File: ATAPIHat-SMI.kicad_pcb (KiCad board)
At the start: 2 copper layers, 65 x 56 mm, 35 parts, among them J1 Pi, J2 IDE, U1 AT24CS32, U2 TXS0108EPW, U3 MCP23S17_SO, U4 MCP23S17_SO

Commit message: Do layout
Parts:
- removed ? (x4): , RPi_Hat:RPi_Hat_Mounting_Hole
- removed D2, D3: Red, LED_SMD:LED_0603_1608Metric
- removed D4, D5: Yellow, LED_SMD:LED_0603_1608Metric
- removed D6, D7: Green, LED_SMD:LED_0603_1608Metric
- removed D8, D9: Blue, LED_SMD:LED_0603_1608Metric
- removed U1: AT24CS32, Package_SO:SOIC-8_3.9x4.9mm_P1.27mm
- removed U2: TXS0108EPW, Package_SO:TSSOP-20_4.4x6.5mm_P0.65mm
- removed U3, U4: MCP23S17_SO, Package_SO:SOIC-28W_7.5x17.9mm_P1.27mm
- added C6: 22uF, Capacitor_SMD:C_0805_2012Metric, F.Cu at (78.8, 159.9)
- added J3: Conn_01x03_Male, Jumper:SolderJumper-3_P1.3mm_Bridged12_Pad1.0x1.5mm, F.Cu at (52.0, 141.9)
- added R12: 33R, Resistor_SMD:R_0402_1005Metric, F.Cu at (100.2, 139.0)
- added R13: 33R, Resistor_SMD:R_0402_1005Metric, F.Cu at (71.0, 136.2)
- added R14: 22R, Resistor_SMD:R_0402_1005Metric, F.Cu at (74.8, 139.0)
- added R15: 33R, Resistor_SMD:R_0402_1005Metric, F.Cu at (99.0, 136.2)
- added R16: 10k, Resistor_SMD:R_0402_1005Metric, F.Cu at (63.4, 139.0)
- added R17: 4.7k, Resistor_SMD:R_0402_1005Metric, F.Cu at (77.3, 139.0)
- added R18: 10k, Resistor_SMD:R_0402_1005Metric, F.Cu at (69.7, 136.2)
- added R19: 5.6k, Resistor_SMD:R_0402_1005Metric, F.Cu at (83.7, 136.2)
- added R20: 75R, Resistor_SMD:R_0402_1005Metric, F.Cu at (86.3, 136.2)
- added R21: 33R, Resistor_SMD:R_0402_1005Metric, F.Cu at (55.8, 136.2)
- added R22: 33R, Resistor_SMD:R_0402_1005Metric, F.Cu at (60.9, 136.2)
- added R23: 22R, Resistor_SMD:R_0402_1005Metric, F.Cu at (91.4, 136.2)
- added R24: 33R, Resistor_SMD:R_0402_1005Metric, F.Cu at (82.5, 139.0)
- added R25: 33R, Resistor_SMD:R_0402_1005Metric, F.Cu at (76.1, 136.2)
- added R26: 33R, Resistor_SMD:R_0402_1005Metric, F.Cu at (92.6, 139.0)
- added R27: 33R, Resistor_SMD:R_0402_1005Metric, F.Cu at (87.5, 139.0)
- added R28: 33R, Resistor_SMD:R_0402_1005Metric, F.Cu at (58.4, 136.2)
- added R29: 33R, Resistor_SMD:R_0402_1005Metric, F.Cu at (88.8, 136.2)
- added R30: 22R, Resistor_SMD:R_0402_1005Metric, F.Cu at (85.0, 139.0)
- added R31: 33R, Resistor_SMD:R_0402_1005Metric, F.Cu at (78.7, 136.2)
- added R32: 33R, Resistor_SMD:R_0402_1005Metric, F.Cu at (81.2, 136.2)
- added R33: 33R, Resistor_SMD:R_0402_1005Metric, F.Cu at (93.9, 136.2)
- C1: value 100n -> 100nF
- C2, C3, C4, C5: value 100n -> 22uF; footprint Capacitor_SMD:C_0402_1005Metric -> Capacitor_SMD:C_0805_2012Metric
- R1, R10, R11, R2, R4, R5, R6: value 4.7k -> 33R
- R7: value 4.7k -> 75R
- R8: value 10k -> 75R
- R9: value 10k -> 33R
- moved R3 53.9 mm to (52.0, 180.6), turned to 0 degrees
- moved D1 53.8 mm to (55.6, 180.6)
- moved J2 47.9 mm to (102.1, 172.3), turned to 270 degrees
- moved R1 34.3 mm to (64.7, 139.0), turned to 90 degrees
- moved R2 33.1 mm to (66.0, 136.2), turned to 90 degrees
- moved C5 32.1 mm to (78.8, 161.8)
- moved C3 24.5 mm to (78.8, 165.6), turned to 0 degrees
- moved C4 23.8 mm to (78.8, 163.7), turned to 0 degrees
- moved R9 23.8 mm to (62.1, 139.0), turned to 90 degrees
- moved R8 20.8 mm to (68.5, 136.2)
- moved C2 18.8 mm to (78.8, 167.5)
- moved R10 18.2 mm to (97.7, 139.0), turned to 90 degrees
- moved R6 18.2 mm to (72.3, 139.0), turned to 90 degrees
- moved R5 17.2 mm to (102.8, 139.0), turned to 90 degrees
- moved R11 17.1 mm to (67.2, 139.0), turned to 90 degrees
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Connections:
- C1 pad 1: +5V -> +3V3
- C2 pad 1: +5V -> /VDRIVE
- C3 pad 1: +5V -> /VDRIVE
- C4 pad 1: +3V3 -> /VDRIVE
- C5 pad 1: +3V3 -> /VDRIVE
- D1 pad 2: +5V -> +3V3
- J1 pad 19: /3V_MOSI -> Net-(J1-Pad19)
- J1 pad 21: /3V_MISO -> Net-(J1-Pad21)
- J1 pad 23: /3V_SCK -> Net-(J1-Pad23)
- J1 pad 24: /3V_CE0 -> Net-(J1-Pad24)
- J1 pad 26: /3V_CE1 -> Net-(J1-Pad26)
- J1 pad 27: /ID_SD -> Net-(J1-Pad27)
- J1 pad 28: /ID_SC -> Net-(J1-Pad28)
- J2 pad 1: +5V -> /RESET
- J2 pad 20: Net-(J2-Pad20) -> /VDRIVE
- J2 pad 21: +5V -> /DMA_RQ
- J2 pad 28: Net-(J2-Pad28) -> GND
- J2 pad 29: +5V -> /DMA_ACK
- R1 pad 1: +3V3 -> /D7
- R1 pad 2: /ID_SD -> Net-(J1-Pad10)
- R10 pad 1: Net-(D8-Pad1) -> /D8
- R10 pad 2: Net-(R10-Pad2) -> Net-(J1-Pad36)
- R11 pad 1: Net-(D9-Pad1) -> /D10
- R11 pad 2: Net-(R11-Pad2) -> Net-(J1-Pad12)
- R2 pad 1: +3V3 -> /D9
- R2 pad 2: /ID_SC -> Net-(J1-Pad11)
- R3 pad 1: Net-(D1-Pad1) -> /ACTIVE
- R3 pad 2: /ACTIVE -> Net-(D1-Pad1)
- R4 pad 1: Net-(D2-Pad1) -> /D11
- R4 pad 2: Net-(R4-Pad2) -> Net-(J1-Pad35)
- R5 pad 1: Net-(D3-Pad1) -> /D13
- R5 pad 2: Net-(R5-Pad2) -> Net-(J1-Pad40)
- R6 pad 1: Net-(D4-Pad1) -> /D15
- R6 pad 2: Net-(R6-Pad2) -> Net-(J1-Pad16)
- R7 pad 1: Net-(D5-Pad1) -> Net-(J1-Pad22)
- R7 pad 2: Net-(R7-Pad2) -> /IO_CH_RD
- R8 pad 1: Net-(D6-Pad1) -> Net-(J1-Pad13)
- R8 pad 2: Net-(R8-Pad2) -> /IRQ
- R9 pad 1: Net-(D7-Pad1) -> /D6
- R9 pad 2: Net-(R9-Pad2) -> Net-(J1-Pad8)
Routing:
- net +5V: track 202.0 -> 15.0 mm, vias 3 -> 0
- net /VDRIVE: track 0.00 -> 70.3 mm, vias 0 -> 5
- net /D9: track 10.4 -> 68.5 mm, vias 0 -> 2
- net /MISO: track 53.3 -> 0.00 mm, vias 3 -> 0
- net /D10: track 10.9 -> 62.0 mm, vias 0 -> 2
- net /CS1: track 18.8 -> 68.5 mm, vias 0 -> 2
- net /MOSI: track 48.4 -> 0.00 mm, vias 5 -> 0
- net /SCK: track 46.7 -> 0.00 mm, vias 4 -> 0
- net /DMA_RQ: track 0.00 -> 45.1 mm, vias 0 -> 2
- net /D6: track 23.3 -> 67.9 mm, vias 0 -> 2
- net /D7: track 23.4 -> 68.0 mm, vias 0 -> 2
- net /DA0: track 20.9 -> 65.4 mm, vias 0 -> 2
- net /IO_CH_RD: track 0.00 -> 43.8 mm, vias 0 -> 2
- net /CE0: track 42.4 -> 0.00 mm, vias 4 -> 0
- net /IOR: track 13.8 -> 55.2 mm, vias 0 -> 2
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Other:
- board text added: "3.3V"
- board text added: "5V"
- board text added: "ATA/ATAPI Hat SMI Rev. A 2020 Tobias Mädel Tobias Schramm"
- board text added: "Activity"
- board text removed: "ATA/ATAPI Hat Rev. B Tobias Mädel 2020"

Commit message: Center hat name
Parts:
- removed C3, C4, C5, C6: 22uF, Capacitor_SMD:C_0805_2012Metric
- added ?: , RPi_Hat:RPi_Hat_Mounting_Hole, F.Cu at (48.4, 131.7)
- added ?: , RPi_Hat:RPi_Hat_Mounting_Hole, F.Cu at (106.4, 180.7)
- added ?: , RPi_Hat:RPi_Hat_Mounting_Hole, F.Cu at (48.4, 180.7)
- added ?: , RPi_Hat:RPi_Hat_Mounting_Hole, F.Cu at (106.4, 131.7)
- moved R3 0.63 mm to (52.6, 180.6)
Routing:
- net /VDRIVE: track 70.3 -> 61.7 mm
- net Net-(D1-Pad1): track 2.69 -> 2.05 mm
- net GND: vias 170 -> 164

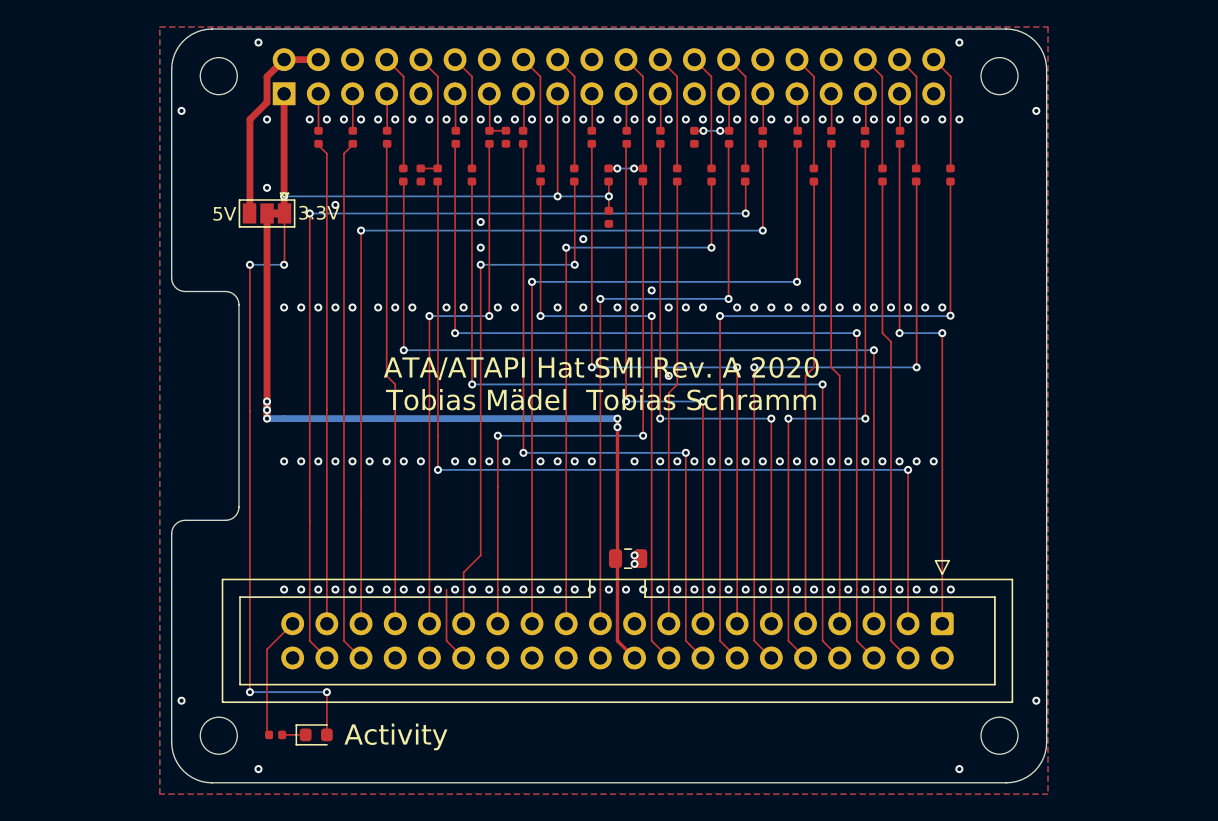
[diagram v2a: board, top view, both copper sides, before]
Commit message: Add tooling holes
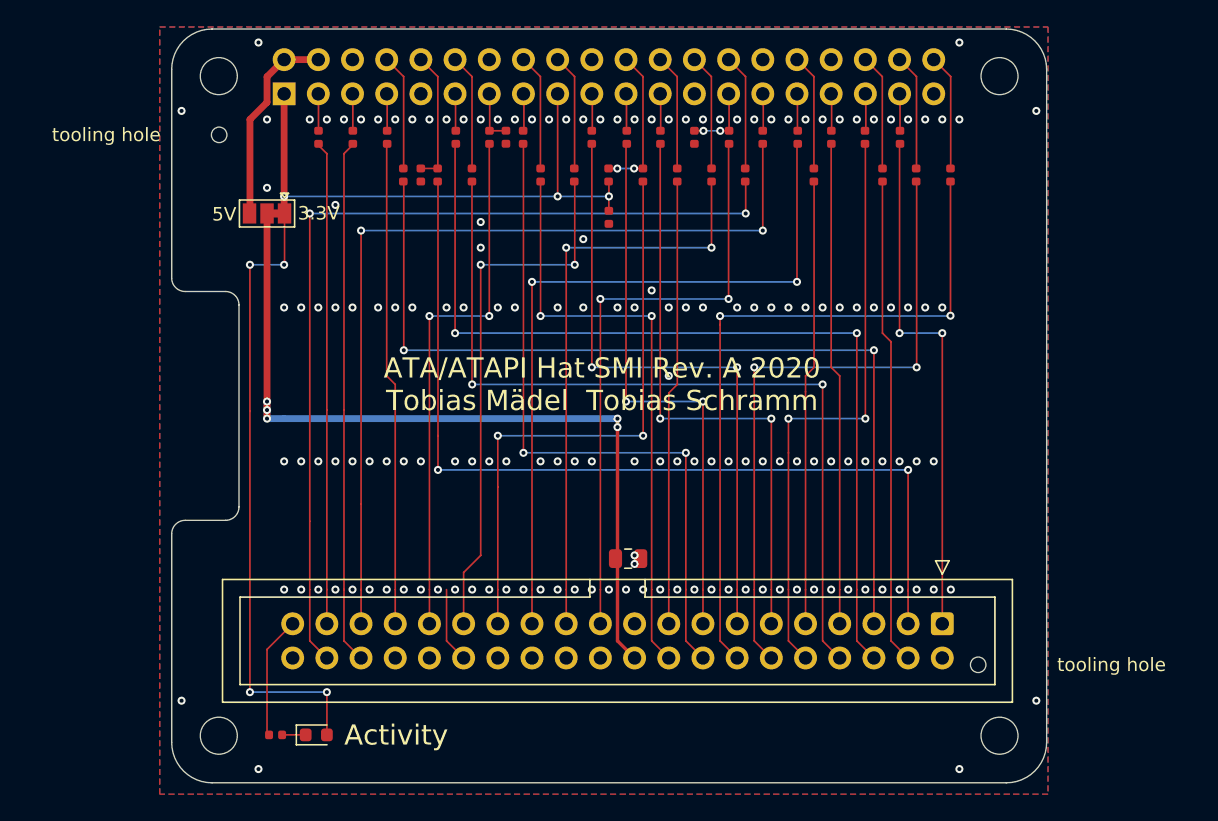
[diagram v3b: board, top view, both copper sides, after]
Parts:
- added H1: ToolingHole, ToolingHole:ToolingHole_JLCSMT, F.Cu at (48.4, 136.0)
- added H2: ToolingHole, ToolingHole:ToolingHole_JLCSMT, F.Cu at (104.8, 175.4)
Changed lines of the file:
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@@
     (tracks 447)
     (zones 0)
-    (modules 43)
+    (modules 45)
     (nets 65)
   )
@@
       (drillshape 0)
       (scaleselection 1)
-      (outputdirectory "IDEHat/"))
+      (outputdirectory "fab"))
   )
   (net 0 "")
@@
     (add_net "Net-(J2-Pad34)")
   )
+  (module ToolingHole:ToolingHole_JLCSMT (layer F.Cu)
+    (at 104.807628 175.387876)
+    (fp_text reference H2 (at 0 0.5) (layer F.SilkS) hide
+      (effects (font (size 1 1) (thickness 0.15)))
+    )
+    (fp_text value ToolingHole (at 0 -0.5) (layer F.Fab)
+      (effects (font (size 1 1) (thickness 0.15)))
+    )
+    (fp_text user "tooling hole" (at 9.906 0) (layer F.SilkS)
+      (effects (font (size 1 1) (thickness 0.15)))
+    )
+    (pad "" np_thru_hole circle (at 0 0) (size 1.152 1.152) (drill 1.152) (layers *.Cu *.Mask))
+  )
+  (module ToolingHole:ToolingHole_JLCSMT (layer F.Cu)
+    (at 48.419628 136.017876)
+    (fp_text reference H1 (at 0 0.5) (layer F.SilkS) hide
+      (effects (font (size 1 1) (thickness 0.15)))
+    )
+    (fp_text value ToolingHole (at 0 -0.5) (layer F.Fab)
+      (effects (font (size 1 1) (thickness 0.15)))
+    )
+    (fp_text user "tooling hole" (at -8.382 0) (layer F.SilkS)
+      (effects (font (size 1 1) (thickness 0.15)))
+    )
+    (pad "" np_thru_hole circle (at 0 0) (size 1.152 1.152) (drill 1.152) (layers *.Cu *.Mask))
+  )
   (module RPi_Hat:RPi_Hat_Mounting_Hole (layer F.Cu)
